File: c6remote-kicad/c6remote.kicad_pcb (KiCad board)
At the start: 2 copper layers, 37 x 130 mm, 46 parts, among them J1 Battery, Q1 MMBT2222A, SW1 SW_Push, SW10 SW_Push, SW11 SW_Push, SW2 SW_Push, SW3 SW_Push, SW4 SW_Push, SW5 SW_Push, SW6 SW_Push, SW7 SW_Push, SW8 SW_Push, SW9 SW_Push, U1 XIAO-ESP32-C6, U2 TSOP4136, U3 PCF8575DBR

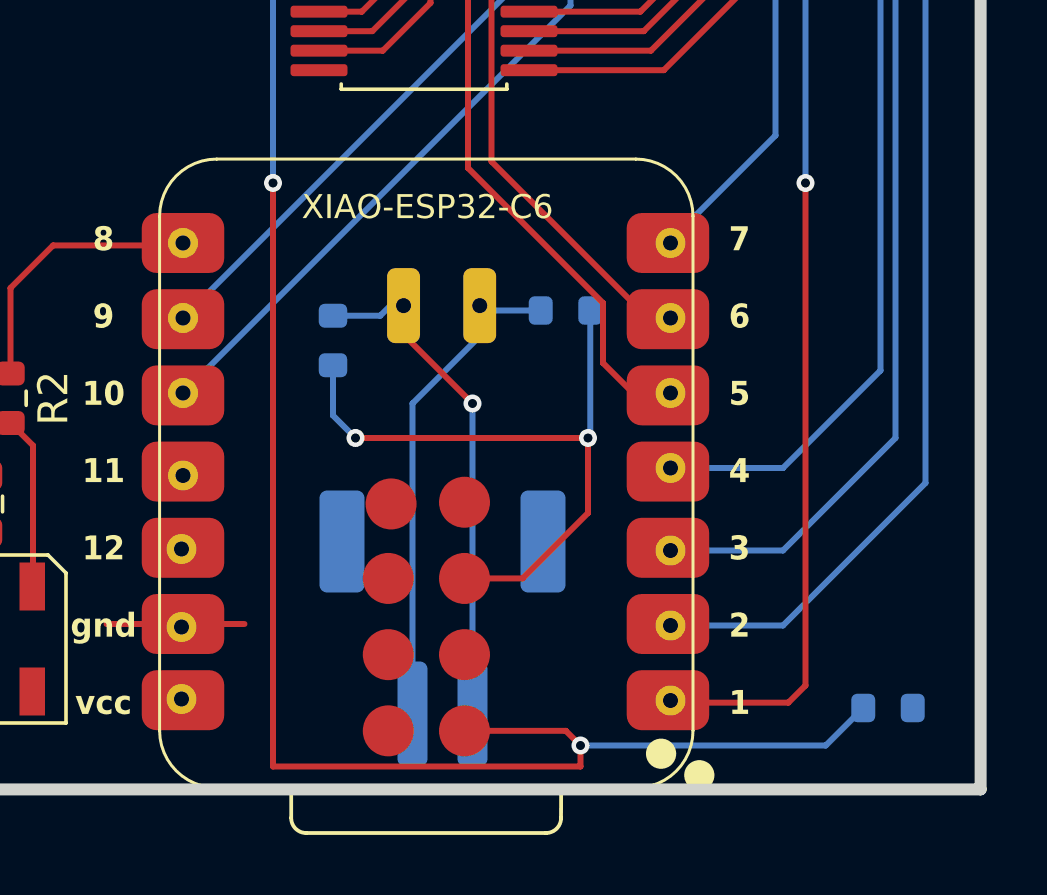
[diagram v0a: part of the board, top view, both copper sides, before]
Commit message: pcb(R9): move INT pull-up from back to front copper at 68.75,155 and reroute +3.3V/BAT/exp_int with 2 new vias, zones refilled and DRC clean (0 unconnected)
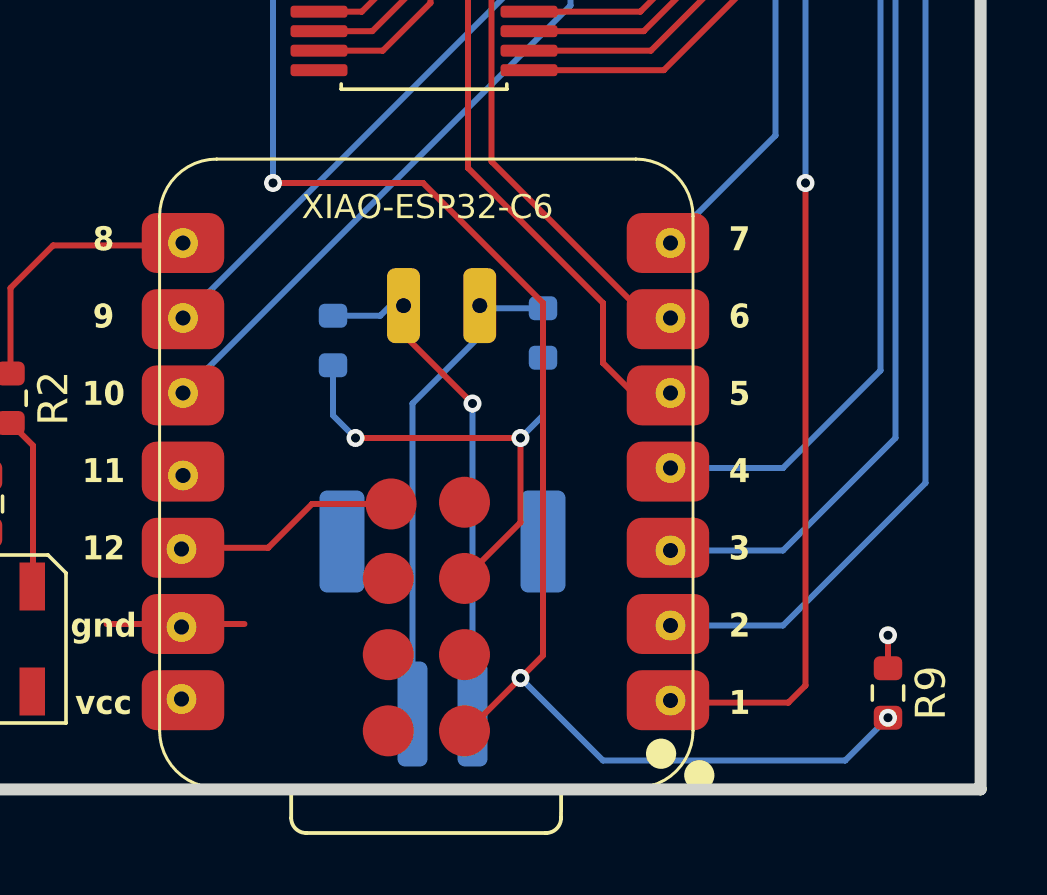
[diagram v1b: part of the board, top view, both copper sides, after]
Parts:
- R9: moved to F.Cu
- moved R7 1.06 mm to (57.2, 143.0), turned to -90 degrees
- moved R9 0.50 mm to (68.8, 155.0), turned to -90 degrees
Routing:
- net +3.3V: track 17.1 -> 25.9 mm, vias 3 -> 4
- net bat_sense: track 22.3 -> 16.7 mm
- net exp_int: track 57.5 -> 53.4 mm, vias 3 -> 4

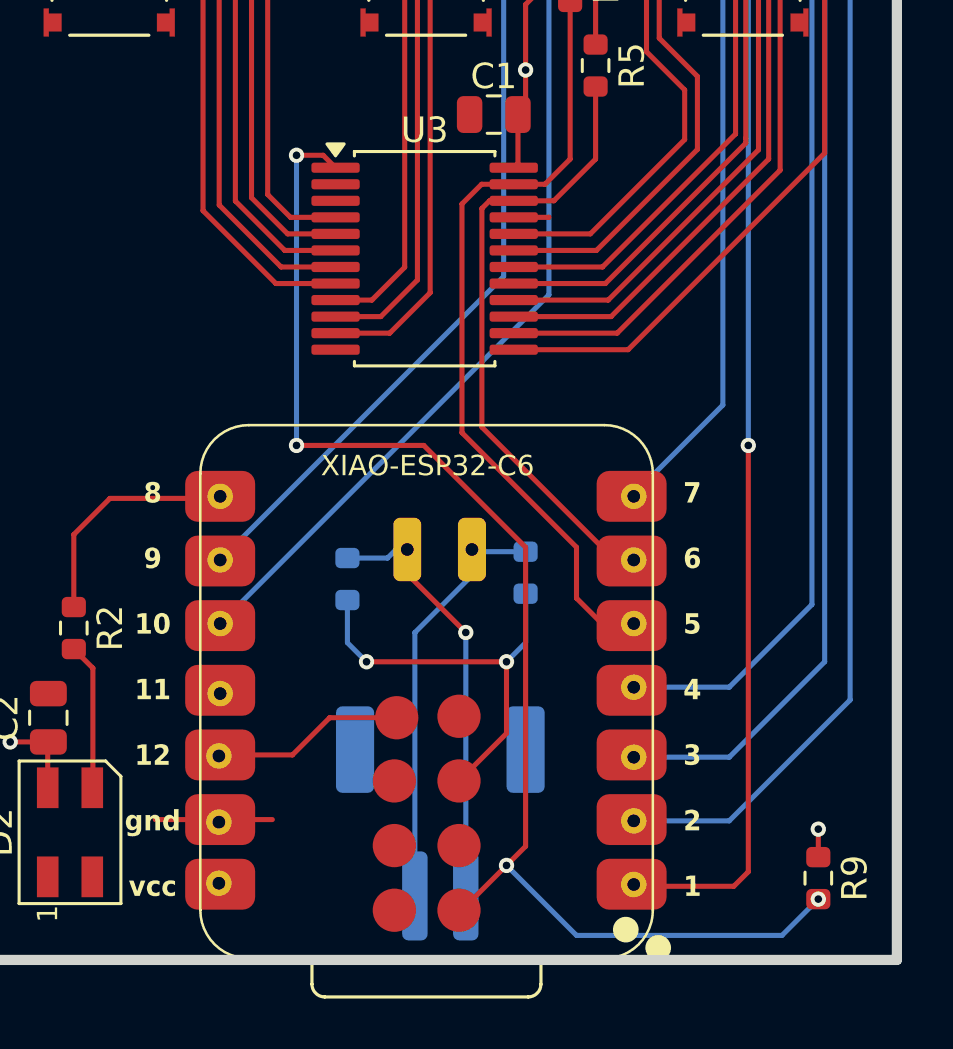
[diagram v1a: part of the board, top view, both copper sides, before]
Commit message: pcb+sch(gnd13): connect U1 pad 13 and TP_GND to F.Cu zone via pad connection fix and refill (45deg thermal spokes were choked by pad 12/14 clearance on 2.54 pitch), convert 4 local GND labels to global, drop stale no-connect on U3 INT exp_int pin; ERC 13 to 12, DRC 0 unconnected
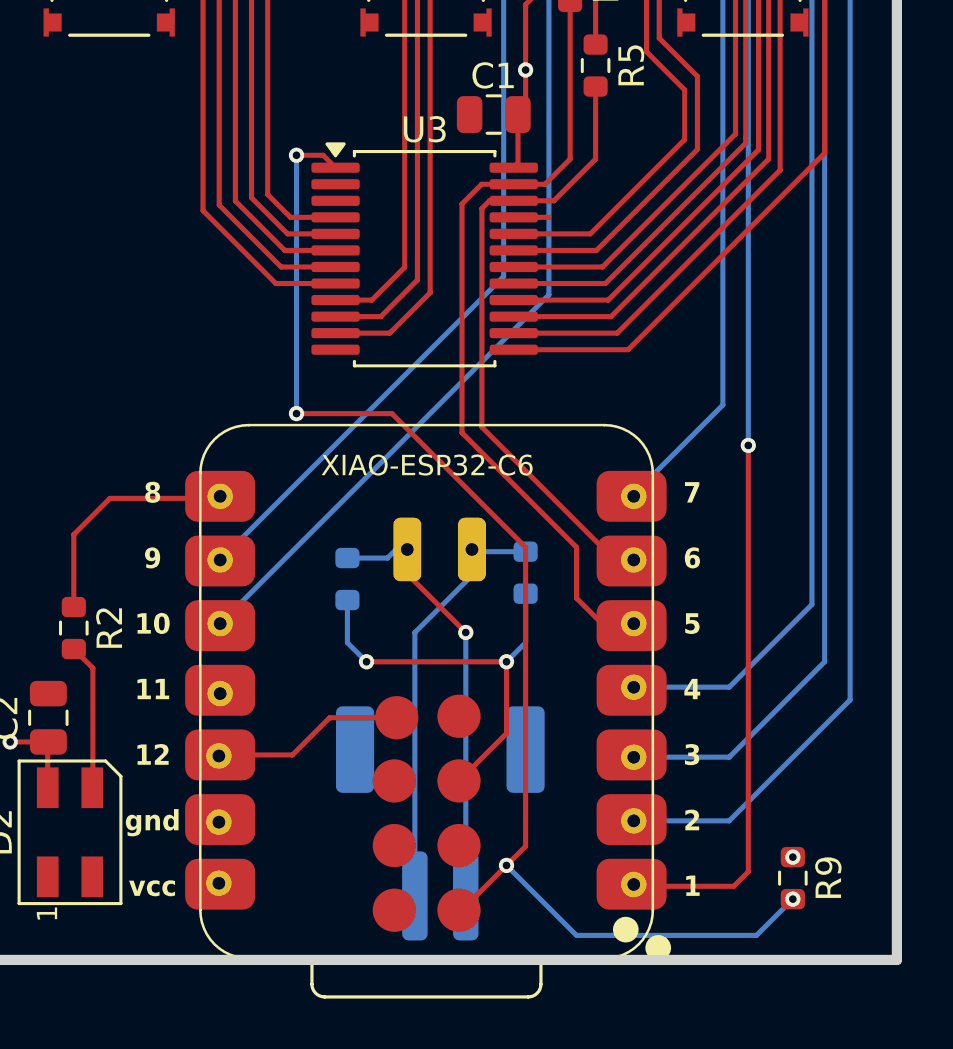
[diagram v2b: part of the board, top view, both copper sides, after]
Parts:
- moved R9 1.00 mm to (67.8, 155.0)
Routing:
- net GND: track 26.5 -> 21.9 mm
- net exp_int: track 53.4 -> 51.4 mm
- net +3.3V: track 25.9 -> 24.7 mm
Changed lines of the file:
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@@
 			(pintype "passive")
 			(solder_mask_margin 0.0508)
+			(zone_connect 2)
 			(thermal_bridge_angle 45)
 		)
@@
 	(footprint "Resistor_SMD:R_0603_1608Metric"
 		(layer "F.Cu")
-		(at 68.75 155 -90)
+		(at 67.75 155 -90)
 		(descr "Resistor SMD 0603 (1608 Metric), square (rectangular) end terminal, IPC-7351 nominal, (Body size source: IPC-SM-782 page 72, https://www.pcb-3d.com/wordpress/wp-content/uploads/ipc-sm-782a_amendment_1_and_2.pdf)")
 		(tags "resistor")
@@
 	)
 	(segment
-		(start 68.75 154.175)
-		(end 68.75 153.075)
-		(width 0.2)
-		(layer "F.Cu")
-		(net "+3.3V")
-	)
-	(segment
 		(start 60 119.425)
 		(end 59.5 118.925)
@@
 	)
 	(segment
-		(start 68.825 153.15)
-		(end 68.75 153.075)
-		(width 0.2)
-		(layer "F.Cu")
-		(net "+3.3V")
-	)
-	(segment
 		(start 36.5 33)
 		(end 37.675 33)
@@
 	)
 	(via
-		(at 68.75 153.075)
+		(at 37 149.65)
 		(size 0.6)
 		(drill 0.3)
@@
 	)
 	(via
-		(at 37 149.65)
+		(at 36.5 33)
 		(size 0.6)
 		(drill 0.3)
 		(layers "F.Cu" "B.Cu")
+		(free yes)
 		(net "+3.3V")
 	)
 	(via
-		(at 36.5 33)
+		(at 57.25 123.25)
 		(size 0.6)
 		(drill 0.3)
@@
 	)
 	(via
-		(at 57.25 123.25)
+		(at 67.75 154.175)
 		(size 0.6)
 		(drill 0.3)
 		(layers "F.Cu" "B.Cu")
-		(free yes)
 		(net "+3.3V")
 	)
@@
 		(net "GND")
 	)
-	(segment
-		(start 45.25 152.7)
-		(end 42.7 152.7)
-		(width 0.2)
-		(layer "F.Cu")
-		(net "GND")
-	)
-	(segment
-		(start 45.25 152.7)
-		(end 47.3 152.7)
-		(width 0.2)
-		(layer "F.Cu")
-		(net "GND")
-	)
 	(via
 		(at 53.35 33.35)
@@
 	)
 	(segment
-		(start 57.25 142)
-		(end 53.25 138)
-		(width 0.2)
-		(layer "F.Cu")
-		(net "exp_int")
-	)
-	(segment
-		(start 53.25 138)
-		(end 48.25 138)
-		(width 0.2)
-		(layer "F.Cu")
-		(net "exp_int")
-	)
-	(segment
 		(start 49.784 127.089)
 		(end 49.295 126.6)
@@
 	(segment
 		(start 57.25 153.75)
-		(end 57.25 142)
+		(end 56.5 154.5)
 		(width 0.2)
 		(layer "F.Cu")
@@
 	)
 	(segment
-		(start 68.75 156.075)
-		(end 68.75 155.825)
+		(start 48.25 136.75)
+		(end 52 136.75)
+		(width 0.2)
+		(layer "F.Cu")
+		(net "exp_int")
+	)
+	(segment
+		(start 52 136.75)
+		(end 57.25 142)
 		(width 0.2)
 		(layer "F.Cu")
@@
 	)
 	(segment
-		(start 56.5 154.5)
+		(start 57.25 142)
 		(end 57.25 153.75)
 		(width 0.2)
@@
 	)
 	(via
-		(at 68.75 155.825)
+		(at 67.75 155.825)
 		(size 0.6)
 		(drill 0.3)
@@
 	)
 	(via
-		(at 48.25 138)
+		(at 48.25 136.75)
 		(size 0.6)
 		(drill 0.3)
@@
 	)
 	(segment
-		(start 56.5 154.5)
-		(end 59.25 157.25)
+		(start 66.325 157.25)
+		(end 67.75 155.825)
 		(width 0.2)
 		(layer "B.Cu")
@@
 	(segment
 		(start 59.25 157.25)
-		(end 67.325 157.25)
+		(end 66.325 157.25)
 		(width 0.2)
 		(layer "B.Cu")
@@
 	(segment
 		(start 48.25 126.6)
-		(end 48.25 138)
+		(end 48.25 136.75)
 		(width 0.2)
 		(layer "B.Cu")
@@
 	)
 	(segment
-		(start 67.325 157.25)
-		(end 68.75 155.825)
+		(start 56.5 154.5)
+		(end 59.25 157.25)
 		(width 0.2)
 		(layer "B.Cu")

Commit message: style(sch): center vertical justification on all 26 labels (drop top/bottom keyword, keep left/right); rename test point TP_VCC->TP_VCC1 on schematic+board so KiCad annotation is stable and parity matches - ERC 0, netlist node TP_VCC1, parity 45, no copper change
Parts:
- renumbered TP_VCC to TP_VCC1
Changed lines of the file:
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@@
 		(descr "THT rectangular pad as test Point, square 1.0mm side length, hole diameter 0.5mm")
 		(tags "test point THT pad rectangle square")
-		(property "Reference" "TP_VCC"
+		(property "Reference" "TP_VCC1"
 			(at 0 -1.448 0)
 			(layer "B.SilkS")

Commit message: fix(anorotary): swap ENC1 pad 6/8 to datasheet functions (COM_A/S4_UP) fixing dead center press + rotation - symbol pins renamed COM_A/COM_B/S1-S5/ENCA/ENCB with pin numbers 6/8 swapped, library+embedded sch copies synced, board pads resynced (pad 6 GND, pad 8 ano_sw2), old pad 6 stub deleted + new F.Cu route to pad 8, zones refilled; ERC 0 DRC 0 parity 45
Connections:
- ENC1 pad 6: ano_sw2 -> GND
- ENC1 pad 8: GND -> ano_sw2
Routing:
- net ano_sw2: track 89.8 -> 95.8 mm
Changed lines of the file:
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@@
 			(layers "*.Cu" "*.Mask")
 			(remove_unused_layers no)
-			(net "ano_sw2")
+			(net "GND")
 			(pinfunction "ano_sw2_6")
 			(pintype "output")
@@
 			(remove_unused_layers no)
 			(roundrect_rratio 0.1)
-			(net "GND")
+			(net "ano_sw2")
 			(pinfunction "COM1_8")
 			(pintype "passive")
@@
 	)
 	(segment
+		(start 45.587565 54.731565)
+		(end 45.587565 52.610131)
+		(width 0.2)
+		(layer "F.Cu")
+		(net "ano_sw2")
+	)
+	(segment
 		(start 65.9 105.856943)
 		(end 66.25 105.506943)
@@
 	)
 	(segment
-		(start 66.25 91.738)
-		(end 68.834 89.154)
+		(start 52.022136 61.166136)
+		(end 45.587565 54.731565)
 		(width 0.2)
 		(layer "F.Cu")
@@
 	)
 	(segment
-		(start 52.022136 61.166136)
-		(end 46.789646 61.166136)
+		(start 66.25 91.738)
+		(end 68.834 89.154)
 		(width 0.2)
 		(layer "F.Cu")

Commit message: fix(pcb): add TP_VCC1 test point footprint on VCC rail matching schematic symbol - single THT probe pad at (45.2, 155.25), pad net VCC, resolves duplicate-refdes/parity so board and sch agree 1:1 on TP_VCC1; DRC shows TP_VCC1 in zero unconnected and zero parity items (remaining 82 DRC / 13 parity are the known SW1-11 terminal-mapping divergence, unchanged)
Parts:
- TP_VCC1: moved to F.Cu
- moved TP_VCC1 0.05 mm to (45.2, 155.2)
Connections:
- SW1 pad 2: sw1 -> GND
- SW1 pad 3: (no net) -> sw1
- SW1 pad 4: (no net) -> sw1
- SW10 pad 2: sw10 -> GND
- SW10 pad 3: (no net) -> sw10
- SW10 pad 4: (no net) -> sw10
- SW11 pad 2: sw11 -> GND
- SW11 pad 3: (no net) -> sw11
- SW11 pad 4: (no net) -> sw11
- SW2 pad 2: sw2 -> GND
- SW2 pad 3: (no net) -> sw2
- SW2 pad 4: (no net) -> sw2
- SW3 pad 2: sw3 -> GND
- SW3 pad 3: (no net) -> sw3
- SW3 pad 4: (no net) -> sw3
- SW4 pad 2: sw4 -> GND
- SW4 pad 3: (no net) -> sw4
- SW4 pad 4: (no net) -> sw4
- SW5 pad 2: sw5 -> GND
- SW5 pad 3: (no net) -> sw5
- SW5 pad 4: (no net) -> sw5
- SW6 pad 2: sw6 -> GND
- SW6 pad 3: (no net) -> sw6
- SW6 pad 4: (no net) -> sw6
- SW7 pad 2: sw7 -> GND
- SW7 pad 3: (no net) -> sw7
- SW7 pad 4: (no net) -> sw7
- SW8 pad 2: sw8 -> GND
- SW8 pad 3: (no net) -> sw8
- SW8 pad 4: (no net) -> sw8
- SW9 pad 2: sw9 -> GND
- SW9 pad 3: (no net) -> sw9
- SW9 pad 4: (no net) -> sw9
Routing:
- net exp_int: track 51.4 -> 52.3 mm

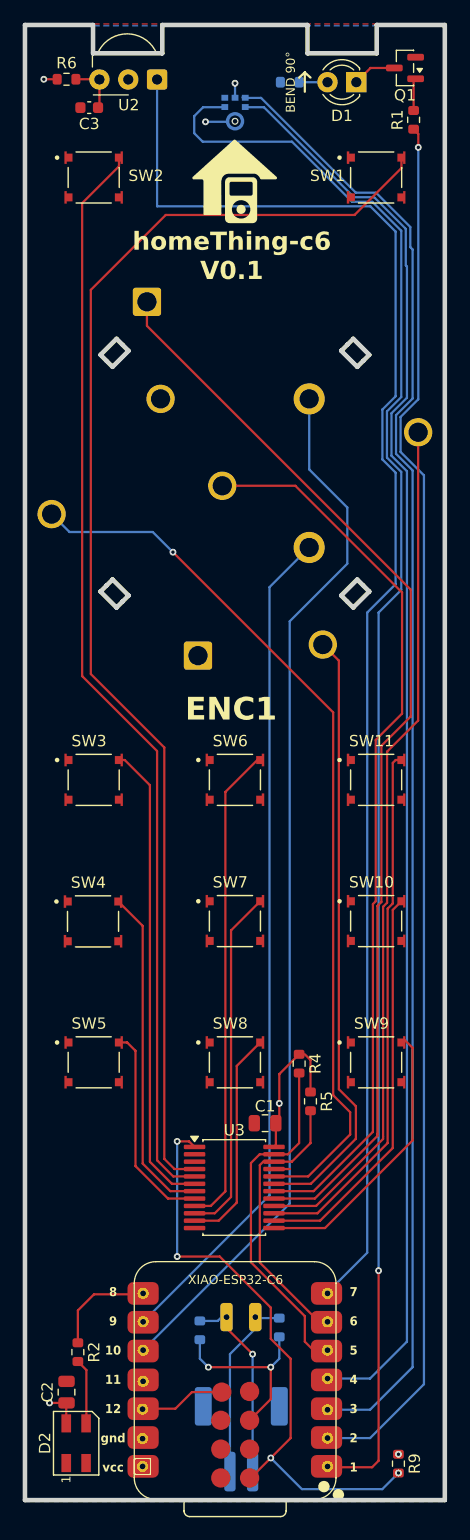
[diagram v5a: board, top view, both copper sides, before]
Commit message: fix(pcb): rotate + rewire SW1-11 to datasheet terminal mapping (pads 1,2 GND / 3,4 sw*), clearing the board-vs-schematic divergence - all 11 SW footprints verified pads 1,2 on GND and 3,4 on sw1..sw11 matching sch convention; ERC 0, DRC 0 errors (42 silk/lib warnings), unconnected 23->0, parity 13 remaining are board-only test points unrelated to buttons
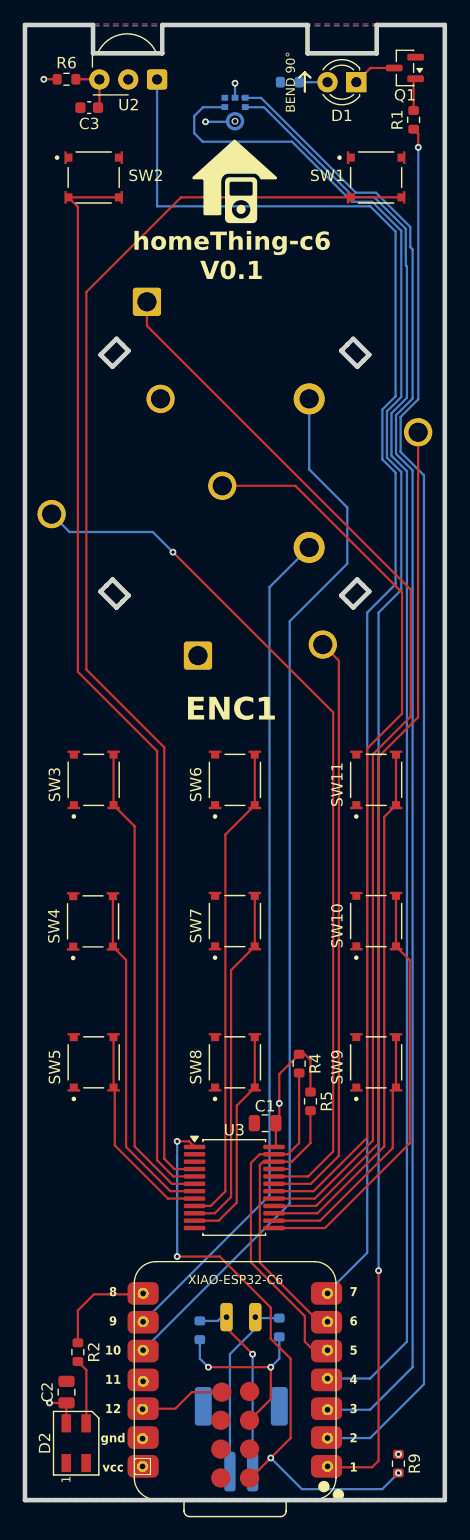
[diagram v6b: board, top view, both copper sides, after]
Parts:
- turned SW10 to 90 degrees
- turned SW11 to 90 degrees
- turned SW3 to 90 degrees
- turned SW4 to 90 degrees
- turned SW5 to 90 degrees
- turned SW6 to 90 degrees
- turned SW7 to 90 degrees
- turned SW8 to 90 degrees
- turned SW9 to 90 degrees
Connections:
- U3 pad 13: sw9 -> sw10
- U3 pad 14: sw10 -> sw9
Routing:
- net sw10: track 35.2 -> 37.4 mm
- net sw9: track 24.6 -> 23.0 mm
- net sw1: track 115.0 -> 113.5 mm
- net ano_sw4: track 53.6 -> 52.4 mm
- net ano_sw5: track 78.1 -> 76.9 mm
- net sw4: track 29.6 -> 30.2 mm

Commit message: fix(pcb): move LED up and battery left to clear room for through-hole center pins, delete leftover led_1 track stub - repositioned D2 (LED) and battery footprint, removed dangling 1.5mm led_1 stub at (46.835,140.0); DRC 0 errors unconnected 0 parity 13, 74 silk/lib warnings from reposition to be cleaned once placement final
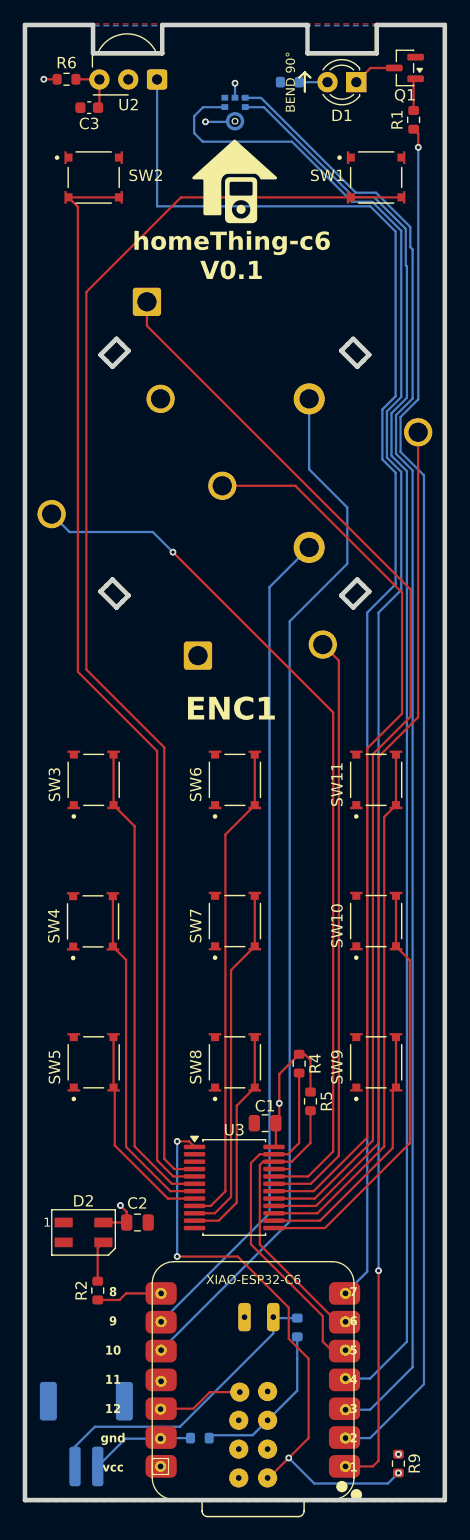
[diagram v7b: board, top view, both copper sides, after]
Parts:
- moved D2 18.6 mm to (40.0, 134.6), turned to 0 degrees
- moved C2 16.2 mm to (44.8, 133.8), turned to 0 degrees
- moved J1 13.7 mm to (40.2, 152.4)
- moved R8 9.50 mm to (50.2, 152.8), turned to 180 degrees
- moved R2 5.70 mm to (41.2, 139.8), turned to 90 degrees
- moved R7 1.59 mm to (58.8, 143.0)
- moved TP_ANO_ENC1 1.59 mm to (46.8, 145.0)
- moved TP_ANO_ENC2 1.59 mm to (46.8, 142.5)
- moved TP_GPIO18_D10_MOSI 1.59 mm to (46.8, 147.8)
- moved TP_IR_EMIT 1.59 mm to (63.1, 152.8)
- moved TP_IR_REC 1.59 mm to (63.1, 140.0)
- moved TP_LED1 1.59 mm to (46.8, 140.0)
- moved TP_SCK 1.59 mm to (63.1, 150.2)
- moved TP_SCL 1.59 mm to (63.1, 142.5)
- moved TP_SD 1.59 mm to (63.1, 155.2)
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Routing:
- net BAT: track 16.6 -> 26.9 mm
- net GND: track 21.9 -> 15.0 mm, vias 3 -> 2
- net led_1: track 9.66 -> 5.82 mm
- net bat_sense: track 16.7 -> 14.2 mm, vias 2 -> 0
- net sd: track 141.9 -> 139.7 mm
- net Net-(D2-DIN): track 5.77 -> 3.63 mm
- net IR EMIT: track 122.8 -> 121.2 mm
- net ws: track 126.2 -> 124.6 mm
- net sck: track 130.3 -> 128.7 mm
- net +3.3V: track 24.7 -> 25.5 mm
- net IR REC: track 130.2 -> 129.5 mm
- net scl: track 24.4 -> 25.0 mm
- net ano_enc1: track 92.6 -> 92.0 mm
- net sda: track 30.8 -> 31.5 mm
- net ano_enc2: track 74.3 -> 73.7 mm
